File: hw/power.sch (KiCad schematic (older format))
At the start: 47 parts, among them J1 Ext_Power, J2 USB_B_Micro, J3 Jtag_Master, Q1 Si3477, U1 TLV62569DDC, U2 TLV62569DDC, U3 TLV62569DDC, U4 FT240XS

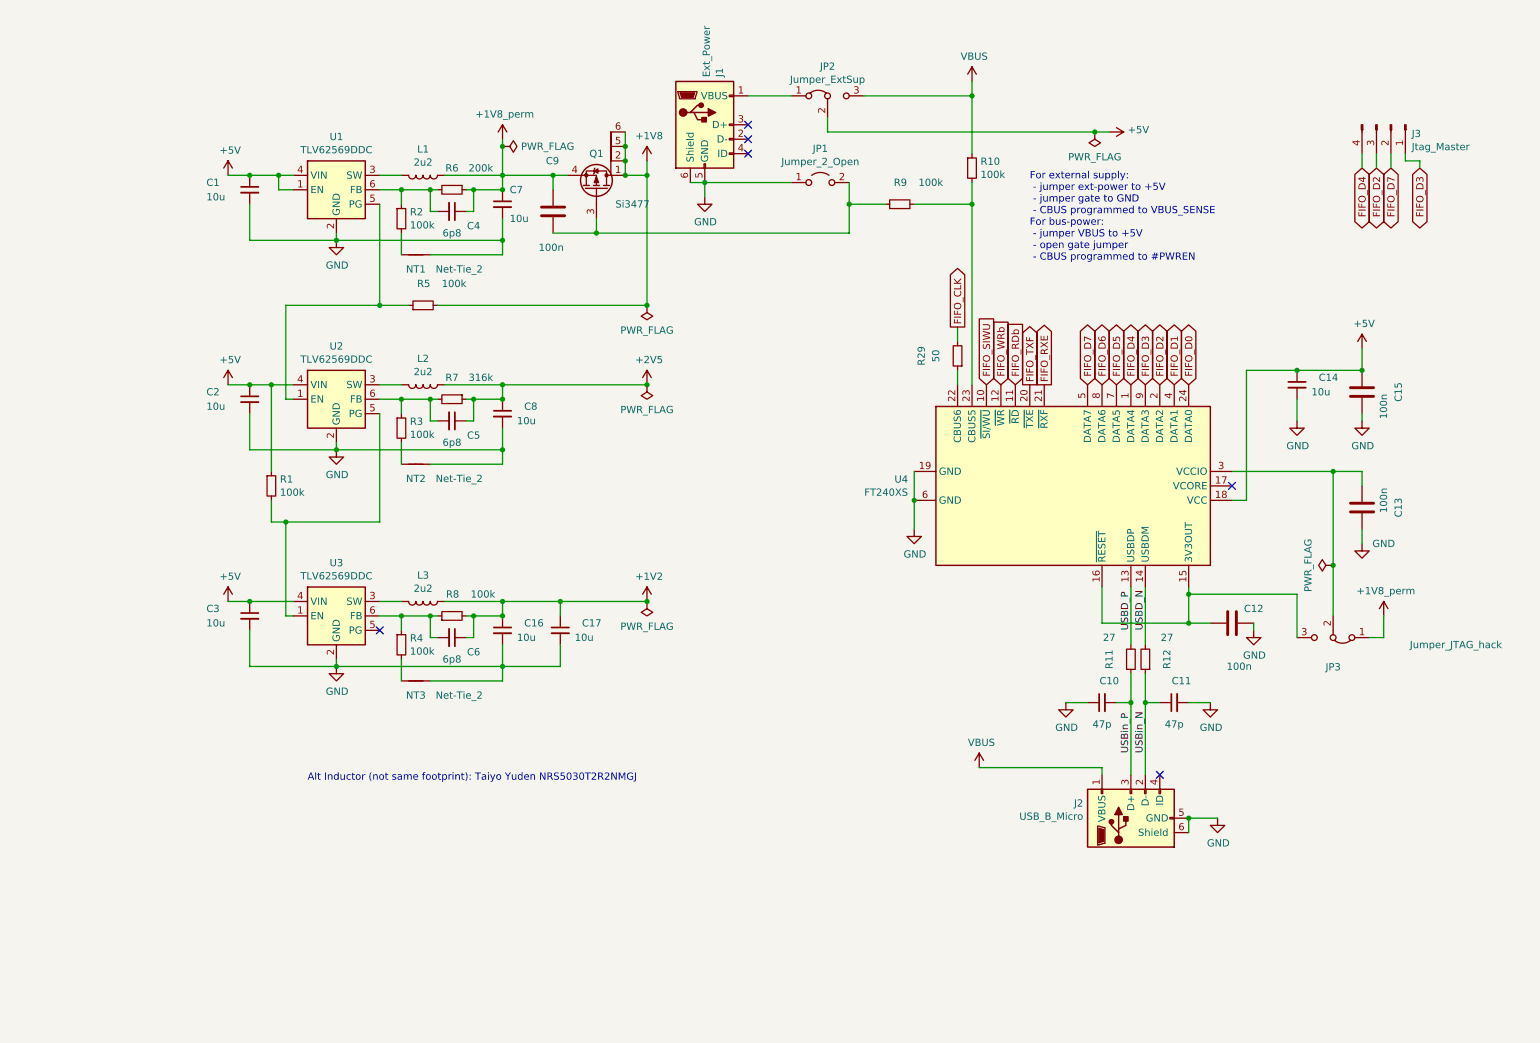
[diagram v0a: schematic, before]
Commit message: Started to work on analog front-end; ADC connected to fpga
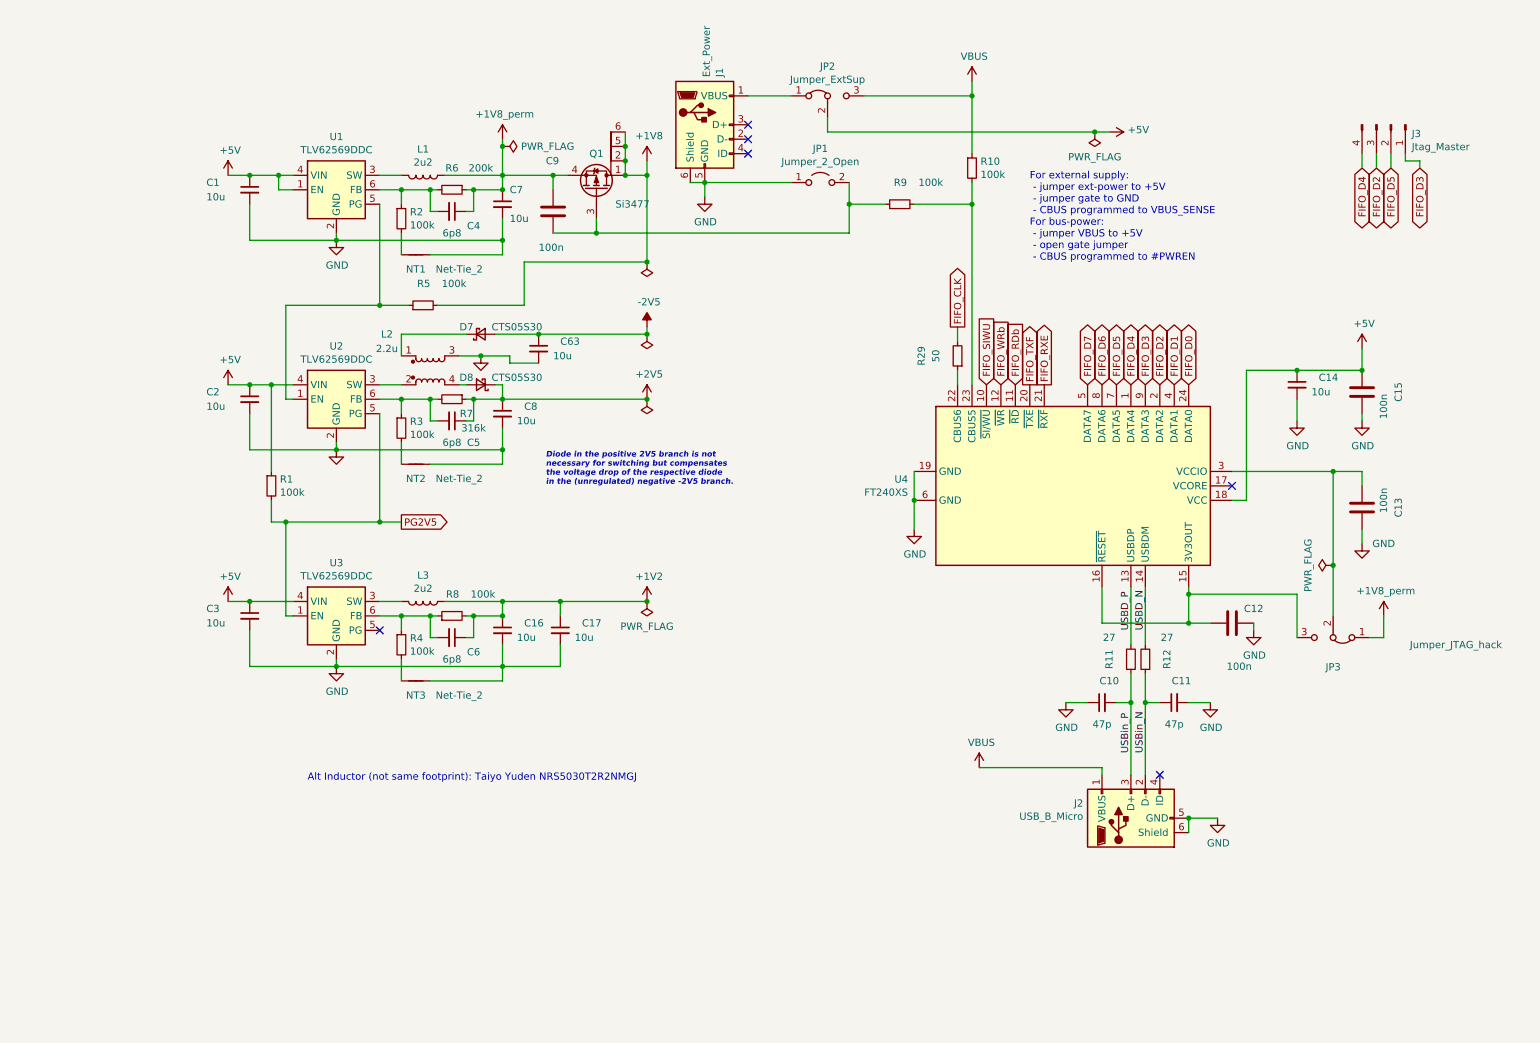
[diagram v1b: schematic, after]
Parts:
- removed L2: 2u2, Inductor_SMD:L_Taiyo-Yuden_NR-50xx, symbol Device:L
- added C63: 10u, Capacitor_SMD:C_1206_3216Metric, symbol Device:C_Small
- added D7: CTS05S30, proj_footprints:sod323, symbol Device:D_Schottky_Small
- added D8: CTS05S30, proj_footprints:sod323-special, symbol Device:D_Schottky_Small
- added L2: 2.2u, proj_footprints:L_Taiyo-Yuden_NR-50xx+bourns0703, symbol Device:L_Coupled_1324
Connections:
- net +2V5: now also D8.1 (K)
- net FIFO_D5: now also J3.2 (Pin_2)
- net FIFO_D7: no longer J3.2 (Pin_2)
- net GND: now also C63.2, L2.3
- net at U2.3 (SW): now also L2.2
- net PG2V5: now reaches R1.2, U2.5 (PG), U3.1 (EN)
- new net: D7.1 (K), L2.1
- new net: D8.2 (A), L2.4
- new net -2V5: C63.1, D7.2 (A)
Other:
- note added: "Diode in the positive 2V5 branch is not\nnecessary for switching but compensates\nthe voltage drop of the respective diode\nin the (unregulated) negative -2V5 branch."
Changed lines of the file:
@@
 $Descr A4 11693 8268
 encoding utf-8
-Sheet 2 4
+Sheet 2 7
 Title ""
 Date ""
@@
 P 2800 3650
 F 0 "#PWR?" H 2800 3400 50  0001 C CNN
-F 1 "GND" H 2805 3477 50  0000 C CNN
+F 1 "GND" H 2805 3477 50  0001 C CNN
 F 2 "" H 2800 3650 50  0001 C CNN
 F 3 "" H 2800 3650 50  0001 C CNN
@@
 Wire Wire Line
 	3250 3300 3250 3400
-$Comp
-L Device:R_Small R7
-U 1 1 6088C3B0
-P 3600 3300
-F 0 "R7" V 3450 3300 50  0000 C CNN
-F 1 "316k" V 3450 3500 50  0000 C CNN
-F 2 "Resistor_SMD:R_0603_1608Metric" H 3600 3300 50  0001 C CNN
-F 3 "~" H 3600 3300 50  0001 C CNN
-F 4 " RC0603FR-07316KL " V 3600 3300 50  0001 C CNN "Part"
-F 5 "Yageo" V 3600 3300 50  0001 C CNN "Manufacturer"
-	1    3600 3300
-	0    1    1    0
-$EndComp
 Wire Wire Line
 	3250 3300 3450 3300
@@
 Connection ~ 3950 3300
 Wire Wire Line
-	3550 3200 3950 3200
-Wire Wire Line
 	3500 3450 3450 3450
 Wire Wire Line
@@
 L power:+2V5 #PWR?
 U 1 1 60893186
-P 4950 3200
-F 0 "#PWR?" H 4950 3050 50  0001 C CNN
-F 1 "+2V5" H 4965 3373 50  0000 C CNN
-F 2 "" H 4950 3200 50  0001 C CNN
-F 3 "" H 4950 3200 50  0001 C CNN
-	1    4950 3200
-	1    0    0    -1
-$EndComp
-Wire Wire Line
-	3950 3200 4950 3200
-Connection ~ 3950 3200
+P 4950 3300
+F 0 "#PWR?" H 4950 3150 50  0001 C CNN
+F 1 "+2V5" H 4965 3473 50  0000 C CNN
+F 2 "" H 4950 3300 50  0001 C CNN
+F 3 "" H 4950 3300 50  0001 C CNN
+	1    4950 3300
+	1    0    0    -1
+$EndComp
+Wire Wire Line
+	3950 3300 4950 3300
 Wire Wire Line
 	2200 3200 2350 3200
@@
 Wire Wire Line
 	2450 3300 2500 3300
-Connection ~ 4950 1750
 $Comp
 L Regulator_Switching:TLV62569DDC U3
@@
 	4600 2150 4600 2050
 Wire Wire Line
-	3500 2650 4950 2650
-Wire Wire Line
-	4950 1750 4950 2650
-Wire Wire Line
 	2450 2650 3100 2650
 Wire Wire Line
@@
 Text Notes 7600 2350 0    50   ~ 0
 For external supply:\n - jumper ext-power to +5V\n - jumper gate to GND\n - CBUS programmed to VBUS_SENSE\nFor bus-power:\n - jumper VBUS to +5V\n - open gate jumper\n - CBUS programmed to #PWREN
-$Comp
-L Device:L L2
-U 1 1 609C00E5
-P 3400 3200
-F 0 "L2" V 3219 3200 50  0000 C CNN
-F 1 "2u2" V 3310 3200 50  0000 C CNN
-F 2 "Inductor_SMD:L_Taiyo-Yuden_NR-50xx" H 3400 3200 50  0001 C CNN
-F 3 "~" H 3400 3200 50  0001 C CNN
-F 4 "SRN8040TA-2R2Y" V 3400 3200 50  0001 C CNN "Part"
-F 5 "Bourns" V 3400 3200 50  0001 C CNN "Manufacturer"
-	1    3400 3200
-	0    1    1    0
-$EndComp
 $Comp
 L Device:L L3
@@
 L power:PWR_FLAG #FLG?
 U 1 1 60A715D8
-P 4950 2650
-F 0 "#FLG?" H 4950 2725 50  0001 C CNN
-F 1 "PWR_FLAG" H 4950 2823 50  0000 C CNN
-F 2 "" H 4950 2650 50  0001 C CNN
-F 3 "~" H 4950 2650 50  0001 C CNN
-	1    4950 2650
+P 4950 2350
+F 0 "#FLG?" H 4950 2425 50  0001 C CNN
+F 1 "PWR_FLAG" H 4950 2523 50  0001 C CNN
+F 2 "" H 4950 2350 50  0001 C CNN
+F 3 "~" H 4950 2350 50  0001 C CNN
+	1    4950 2350
 	1    0    0    1
 $EndComp
-Connection ~ 4950 2650
 $Comp
 L power:PWR_FLAG #FLG?
@@
 	6800 3800 6800 4000
 Connection ~ 6800 4000
-Connection ~ 4950 3200
+Connection ~ 4950 3300
 $Comp
 L power:PWR_FLAG #FLG?
 U 1 1 60A71BDA
-P 4950 3200
-F 0 "#FLG?" H 4950 3275 50  0001 C CNN
-F 1 "PWR_FLAG" H 4950 3373 50  0000 C CNN
-F 2 "" H 4950 3200 50  0001 C CNN
-F 3 "~" H 4950 3200 50  0001 C CNN
-	1    4950 3200
+P 4950 3300
+F 0 "#FLG?" H 4950 3375 50  0001 C CNN
+F 1 "PWR_FLAG" H 4950 3473 50  0001 C CNN
+F 2 "" H 4950 3300 50  0001 C CNN
+F 3 "~" H 4950 3300 50  0001 C CNN
+	1    4950 3300
 	1    0    0    1
 $EndComp
@@
 FIFO_D2
 Text GLabel 10100 1700 3    50   BiDi ~ 0
-FIFO_D7
+FIFO_D5
 Wire Wire Line
 	9900 1600 9900 1700
@@
 U 1 1 60BFDD30
 P 3600 3450
-F 0 "C5" V 3700 3600 50  0000 C CNN
+F 0 "C5" V 3750 3600 50  0000 C CNN
 F 1 "6p8" V 3750 3450 50  0000 C CNN
 F 2 "Capacitor_SMD:C_0603_1608Metric" H 3600 3450 50  0001 C CNN
@@
 Wire Wire Line
 	6200 1450 8050 1450
+Text GLabel 3250 4150 2    50   Output ~ 0
+PG2V5
+Wire Wire Line
+	3250 4150 3100 4150
+Connection ~ 3100 4150
+$Comp
+L Device:R_Small R7
+U 1 1 6088C3B0
+P 3600 3300
+F 0 "R7" V 3700 3400 50  0000 C CNN
+F 1 "316k" V 3800 3450 50  0000 C CNN
+F 2 "Resistor_SMD:R_0603_1608Metric" H 3600 3300 50  0001 C CNN
+F 3 "~" H 3600 3300 50  0001 C CNN
+F 4 " RC0603FR-07316KL " V 3600 3300 50  0001 C CNN "Part"
+F 5 "Yageo" V 3600 3300 50  0001 C CNN "Manufacturer"
+	1    3600 3300
+	0    1    1    0
+$EndComp
+Text Notes 4250 3900 0    39   Italic 8
+Diode in the positive 2V5 branch is not\nnecessary for switching but compensates\nthe voltage drop of the respective diode\nin the (unregulated) negative -2V5 branch.
+$Comp
+L Device:L_Coupled_1324 L2
+U 1 1 60BB27E5
+P 3450 3100
+F 0 "L2" H 3150 3350 50  0000 C CNN
+F 1 "2.2u" H 3150 3250 50  0000 C CNN
+F 2 "proj_footprints:L_Taiyo-Yuden_NR-50xx+bourns0703" H 3450 3100 50  0001 C CNN
+F 3 "~" H 3450 3100 50  0001 C CNN
+F 4 "SRF0703-2R2M" H 3450 3100 50  0001 C CNN "Part"
+F 5 "Bourns" H 3450 3100 50  0001 C CNN "Manufacturer"
+	1    3450 3100
+	1    0    0    -1
+$EndComp
+$Comp
+L Device:D_Schottky_Small D8
+U 1 1 60BB54A7
+P 3800 3200
+F 0 "D8" H 3900 3150 50  0000 C CNN
+F 1 "CTS05S30" H 3550 3150 50  0000 C CNN
+F 2 "proj_footprints:sod323-special" V 3800 3200 50  0001 C CNN
+F 3 "~" V 3800 3200 50  0001 C CNN
+F 4 "CTS05S30" H 3800 3200 50  0001 C CNN "Part"
+F 5 "Toshiba" H 3800 3200 50  0001 C CNN "Manufacturer"
+	1    3800 3200
+	-1   0    0    1
+$EndComp
+Wire Wire Line
+	3650 3200 3700 3200
+Wire Wire Line
+	3900 3200 3950 3200
+$Comp
+L Device:D_Schottky_Small D7
+U 1 1 60BC459F
+P 3800 2850
+F 0 "D7" H 3700 2800 50  0000 C CNN
+F 1 "CTS05S30" H 4050 2800 50  0000 C CNN
+F 2 "proj_footprints:sod323" V 3800 2850 50  0001 C CNN
+F 3 "~" V 3800 2850 50  0001 C CNN
+F 4 "CTS05S30" H 3800 2850 50  0001 C CNN "Part"
+F 5 "Toshiba" H 3800 2850 50  0001 C CNN "Manufacturer"
+	1    3800 2850
+	1    0    0    1
+$EndComp
+Wire Wire Line
+	3250 3000 3250 2850
+Wire Wire Line
+	3250 2850 3700 2850
+$Comp
+L power:GND #PWR?
+U 1 1 60BCCE0F
+P 3800 3000
+F 0 "#PWR?" H 3800 2750 50  0001 C CNN
+F 1 "GND" H 3805 2827 50  0001 C CNN
+F 2 "" H 3800 3000 50  0001 C CNN
+F 3 "" H 3800 3000 50  0001 C CNN
+	1    3800 3000
+	1    0    0    -1
+$EndComp
+Wire Wire Line
+	3650 3000 3800 3000
+$Comp
+L Device:C_Small C63
+U 1 1 60BD4FD9
+P 4200 2950
+F 0 "C63" H 4350 3000 50  0000 L CNN
+F 1 "10u" H 4300 2900 50  0000 L CNN
+F 2 "Capacitor_SMD:C_1206_3216Metric" H 4200 2950 50  0001 C CNN
+F 3 "~" H 4200 2950 50  0001 C CNN
+F 4 "CNC5L1X7R1C106K160AE" H 4200 2950 50  0001 C CNN "Part"
+F 5 "TDK" H 4200 2950 50  0001 C CNN "Manufacturer"
+	1    4200 2950
+	1    0    0    -1
+$EndComp
+Wire Wire Line
+	3900 2850 4200 2850
+Wire Wire Line
+	4200 3050 4000 3050
+Wire Wire Line
+	4000 3050 4000 3000
+Wire Wire Line
+	4000 3000 3800 3000
+Connection ~ 3800 3000
+$Comp
+L power:-2V5 #PWR?
+U 1 1 60BE6299
+P 4950 2800
+F 0 "#PWR?" H 4950 2900 50  0001 C CNN
+F 1 "-2V5" H 4965 2973 50  0000 C CNN
+F 2 "" H 4950 2800 50  0001 C CNN
+F 3 "" H 4950 2800 50  0001 C CNN
+	1    4950 2800
+	1    0    0    -1
+$EndComp
+Wire Wire Line
+	4950 1750 4950 2350
+Connection ~ 4950 1750
+Wire Wire Line
+	4950 2350 4100 2350
+Wire Wire Line
+	4100 2350 4100 2650
+Wire Wire Line
+	4100 2650 3500 2650
+Connection ~ 4950 2350
+Wire Wire Line
+	4200 2850 4950 2850
+Wire Wire Line
+	4950 2850 4950 2800
+Connection ~ 4200 2850
+$Comp
+L power:PWR_FLAG #FLG?
+U 1 1 60C0907B
+P 4950 2850
+F 0 "#FLG?" H 4950 2925 50  0001 C CNN
+F 1 "PWR_FLAG" H 4950 3023 50  0001 C CNN
+F 2 "" H 4950 2850 50  0001 C CNN
+F 3 "~" H 4950 2850 50  0001 C CNN
+	1    4950 2850
+	1    0    0    1
+$EndComp
+Connection ~ 4950 2850
 $EndSCHEMATC

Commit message: more work (don't recall details :-()
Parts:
- removed J2: USB_B_Micro, Connector_USB:USB_Micro-B_Molex-105017-0001, symbol Connector:USB_B_Micro
- added C100: 100n, Capacitor_SMD:C_0603_1608Metric, symbol fmc:100nF_603
- added J11: PEN_SEL, Connector_PinHeader_2.54mm:PinHeader_2x03_P2.54mm_Vertical, symbol Connector_Generic:Conn_02x03_Odd_Even
- added J2: USB_C_Receptacle_USB2.0, proj_footprints:USB_C_Receptacle_GCT_USB4085_smaller_holes, symbol Connector:USB_C_Receptacle_USB2.0
- added R63, R64, R67, R68: 10k, Resistor_SMD:R_0603_1608Metric, symbol Device:R_Small
- added R65, R66, R69: 5k1, Resistor_SMD:R_0603_1608Metric, symbol Device:R_Small
- added R70: 35k7, Resistor_SMD:R_0603_1608Metric, symbol Device:R_Small
- added R71, R72: 100k, Resistor_SMD:R_0603_1608Metric, symbol Device:R_Small
- added U15: UTC2000, Package_DFN_QFN:QFN-16-1EP_3x3mm_P0.5mm_EP1.75x1.75mm_ThermalVias, symbol fmc:UTC2000
- added U16: 74LVC1G32, Package_TO_SOT_SMD:SOT-353_SC-70-5, symbol 74xGxx:74LVC1G32
- R10: value 100k -> 47k
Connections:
- net GND: now also C100.2, J11.6 (Pin_6), J2.A1 (GND), J2.A12 (GND), J2.B1 (GND), J2.B12 (GND), J2.S1 (SHIELD), R65.2, R66.2, R69.2, U15.13 (VSS), U15.17 (EPAD), U16.3 (GND)
- net USBin_N: now also J2.A7 (D-), J2.B7 (D-)
- net USBin_P: now also J2.A6 (D+), J2.B6 (D+)
- net VBUS: now also C100.1, J2.A4 (VBUS), J2.A9 (VBUS), J2.B4 (VBUS), J2.B9 (VBUS), R67.1, R68.1, R70.1, R71.2, U15.16 (VDD), U16.5 (VCC)
- net at C9.1, Q1.3 (G): now also R72.1; no longer JP1.2 (B), R9.1
- net PG2V5: no longer names the net of R1.2, U2.5 (PG), U3.1 (EN)
- new net: JP1.2 (B), R9.1, U16.2
- new net: J2.B5 (CC2), R63.1, R65.1
- new net: R63.2, U15.6 (CC2)
- new net: J2.A5 (CC1), R64.1, R66.1
- new net: R64.2, U15.7 (CC1)
- new net: R67.2, U15.3 (Enable)
- new net: R68.2, U15.2 (CFG_SEL)
- new net: R69.1, R70.2, U15.12 (VMON)
- new net: J11.1 (Pin_1), J11.3 (Pin_3), J11.5 (Pin_5), R71.1, U16.1
- new net: R72.2, U16.4
- new net 1A5: J11.2 (Pin_2), U15.9 (1.5A#)
- new net 3A0: J11.4 (Pin_4), U15.10 (3A#)
- no-connect marks 6 -> 12
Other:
- moved on the sheet: C1, C10, C11, C12, C13, C14, C15, C16, C17, C2, C3, C4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

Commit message: everything hooked up + layed out; 0.2/0.4mm vias :-(
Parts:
- added C101: 100n, Capacitor_SMD:C_0603_1608Metric, symbol fmc:100nF_603
- added FB1, FB3, FB4, FB5: Ferrite_Bead MPZ1608S221A, Inductor_SMD:L_0603_1608Metric, symbol Device:Ferrite_Bead
- added Q2: Si3477, Package_TO_SOT_SMD:TSOT-23-6, symbol fmc:Q_PMOS_DDGSDD
- added R73: 100k, Resistor_SMD:R_0603_1608Metric, symbol Device:R_Small
- U16: symbol 74xGxx:74LVC1G32 -> fmc:74LVC1G32
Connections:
- net +1V8: now also FB4.1
- net +2V5: now also FB3.1
- net +5V: now also R71.2, U16.5 (VCC), C101.2, Q2.4 (S)
- net -2V5: now also FB5.2; no longer C63.1, D7.2 (A)
- net VBUS: no longer R71.2, U16.5 (VCC)
- net PWR_EN: now reaches R72.2, U16.4
- net PWR_EN: now also R73.2
- new net: C63.1, D7.2 (A), FB5.1
- new net: FB1.1, Q2.1 (D), Q2.2 (D), Q2.5 (D), Q2.6 (D)
- new net: C101.1, Q2.3 (G), R73.1
- new net +1V8_analog: FB4.2
- new net +2V5_analog: FB3.2
- new net Vpp_analog: FB1.2

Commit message: prototype version
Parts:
- added J9: Expansion, Connector_PinHeader_2.54mm:PinHeader_2x04_P2.54mm_Vertical, symbol Connector_Generic:Conn_02x04_Odd_Even
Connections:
- net +1V8: now also J9.4 (Pin_4)
- net +2V5: now also J9.6 (Pin_6)
- net +5V: now also J9.8 (Pin_8)
- net GND: now also J9.1 (Pin_1), J9.7 (Pin_7)
- net -2V5_dig: now reaches C63.1, D7.2 (A), FB5.1
- net -2V5_dig: now also J9.2 (Pin_2)
- new net EXP_IO1_1V8: J9.3 (Pin_3)
- new net EXP_IO2_1V8: J9.5 (Pin_5)
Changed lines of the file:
@@
 	1    0    0    -1
 $EndComp
+$Comp
+L power:+5V #PWR?
+U 1 1 61288191
+P 4150 6350
+F 0 "#PWR?" H 4150 6200 50  0001 C CNN
+F 1 "+5V" H 4165 6523 50  0000 C CNN
+F 2 "" H 4150 6350 50  0001 C CNN
+F 3 "" H 4150 6350 50  0001 C CNN
+	1    4150 6350
+	1    0    0    -1
+$EndComp
+$Comp
+L power:+2V5 #PWR?
+U 1 1 61288652
+P 4250 6100
+F 0 "#PWR?" H 4250 5950 50  0001 C CNN
+F 1 "+2V5" H 4265 6273 50  0000 C CNN
+F 2 "" H 4250 6100 50  0001 C CNN
+F 3 "" H 4250 6100 50  0001 C CNN
+	1    4250 6100
+	1    0    0    -1
+$EndComp
+$Comp
+L power:+1V8 #PWR?
+U 1 1 61289696
+P 4350 6350
+F 0 "#PWR?" H 4350 6200 50  0001 C CNN
+F 1 "+1V8" H 4365 6523 50  0000 C CNN
+F 2 "" H 4350 6350 50  0001 C CNN
+F 3 "" H 4350 6350 50  0001 C CNN
+	1    4350 6350
+	1    0    0    -1
+$EndComp
+$Comp
+L power:GND #PWR?
+U 1 1 612BF64B
+P 4150 7450
+F 0 "#PWR?" H 4150 7200 50  0001 C CNN
+F 1 "GND" H 4155 7277 50  0000 C CNN
+F 2 "" H 4150 7450 50  0001 C CNN
+F 3 "" H 4150 7450 50  0001 C CNN
+	1    4150 7450
+	1    0    0    -1
+$EndComp
+Wire Wire Line
+	4150 7000 4150 7450
+Text Label 4450 6350 0    50   ~ 0
+-2V5_dig
+Text Label 3050 2850 0    50   ~ 0
+-2V5_dig
+$Comp
+L power:GND #PWR?
+U 1 1 612E5772
+P 4450 7450
+F 0 "#PWR?" H 4450 7200 50  0001 C CNN
+F 1 "GND" H 4455 7277 50  0000 C CNN
+F 2 "" H 4450 7450 50  0001 C CNN
+F 3 "" H 4450 7450 50  0001 C CNN
+	1    4450 7450
+	1    0    0    -1
+$EndComp
+Wire Wire Line
+	4450 7000 4450 7450
+Wire Wire Line
+	4350 7000 4350 7050
+Wire Wire Line
+	4350 7050 4650 7050
+Wire Wire Line
+	4250 7000 4250 7200
+Wire Wire Line
+	4250 7200 4650 7200
+Text GLabel 4650 7200 2    50   BiDi ~ 0
+EXP_IO2_1V8
+Text GLabel 4650 7050 2    50   BiDi ~ 0
+EXP_IO1_1V8
+$Comp
+L Connector_Generic:Conn_02x04_Odd_Even J9
+U 1 1 613F2449
+P 4350 6800
+F 0 "J9" V 4446 6980 50  0000 L CNN
+F 1 "Expansion" V 4355 6980 50  0000 L CNN
+F 2 "Connector_PinHeader_2.54mm:PinHeader_2x04_P2.54mm_Vertical" H 4350 6800 50  0001 C CNN
+F 3 "~" H 4350 6800 50  0001 C CNN
+	1    4350 6800
+	0    1    -1   0
+$EndComp
+Wire Wire Line
+	4250 6100 4250 6500
+Wire Wire Line
+	4350 6350 4350 6500
+Wire Wire Line
+	4450 6350 4450 6500
+Wire Wire Line
+	4150 6350 4150 6500
 $EndSCHEMATC
